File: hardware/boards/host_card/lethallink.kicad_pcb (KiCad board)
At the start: 6 copper layers, 121.2 x 98.4 mm, 217 parts, among them J1 PCIe-x4, J2 USB3_Micro_B_Amphenol, J3 Conn_02x05_Odd_Even, J4 Conn_02x04_Odd_Even, J5 Conn_02x04_Odd_Even, J6 SODIMM_260, J7 Conn_02x04_Odd_Even, Q1 Q_NMOS_GSD, Q2 Q_NMOS_GSD, Q3 Q_NMOS_GSD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

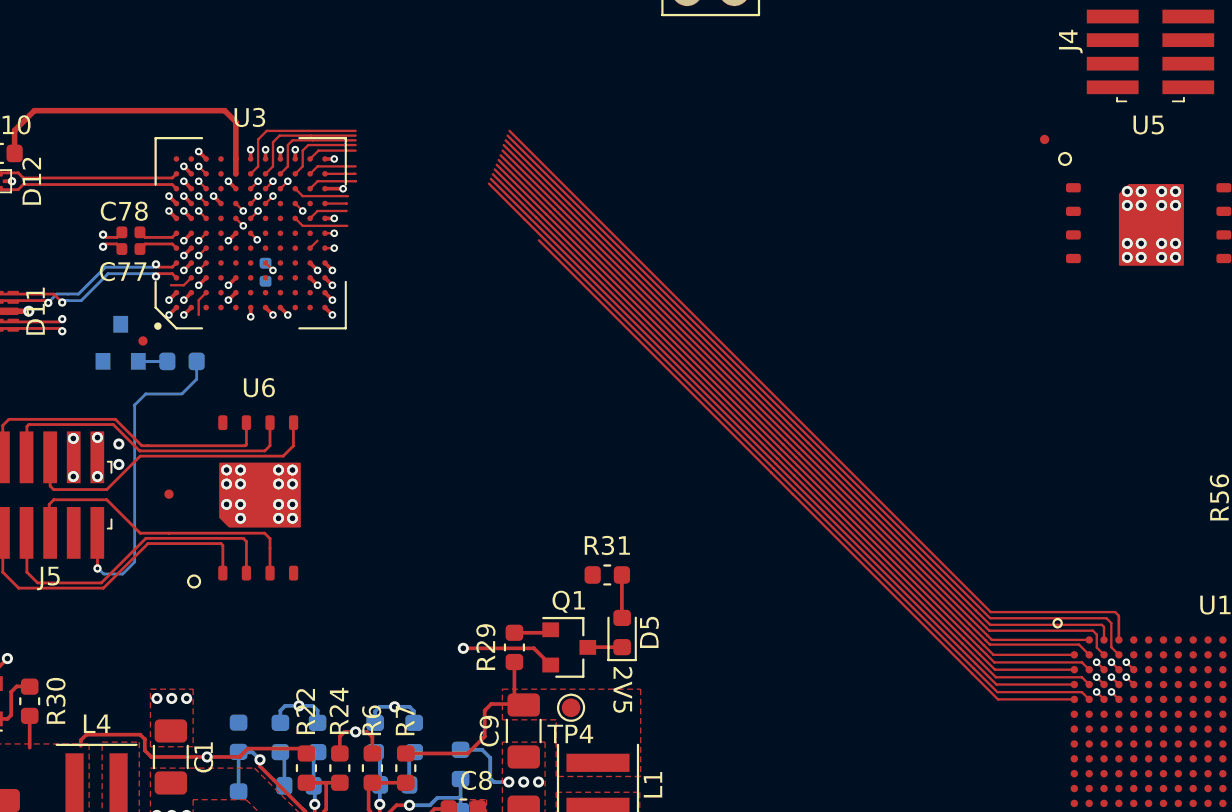
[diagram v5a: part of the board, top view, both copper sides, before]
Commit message: Wiggled all the top traces that needed a good wiggling
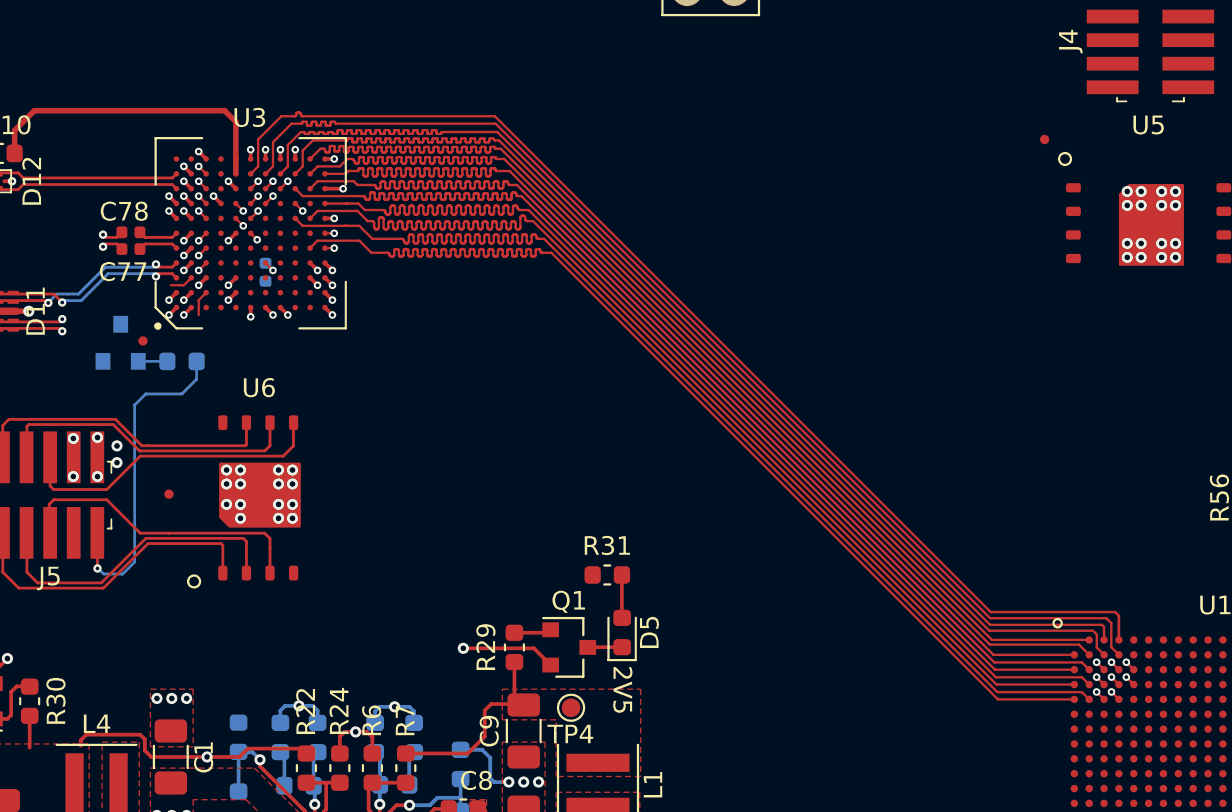
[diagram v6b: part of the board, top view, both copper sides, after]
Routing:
- net /USB3 Interface/ALE: track 39.6 -> 61.5 mm
- net /USB3 Interface/WE_D: track 44.8 -> 63.6 mm
- net /Boot Config/~PHY_INT: track 44.7 -> 62.7 mm
- net /USB3 Interface/DQ11: track 43.7 -> 61.5 mm
- net /USB3 Interface/OE: track 46.8 -> 64.4 mm
- net /USB3 Interface/DQ10: track 45.1 -> 61.6 mm
- net /USB3 Interface/DQ9: track 45.4 -> 61.5 mm
- net /USB3 Interface/DQ12: track 45.4 -> 61.5 mm
- net /USB3 Interface/DQ13: track 45.8 -> 61.5 mm
- net /USB3 Interface/DQ8: track 48.5 -> 61.5 mm
- net /USB3 Interface/DQ6: track 49.2 -> 61.6 mm
- net /USB3 Interface/DQ3: track 51.7 -> 61.5 mm
- net /USB3 Interface/DQ0: track 53.7 -> 62.8 mm

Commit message: Lots of updates from a while ago, don't recall what's changed
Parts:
- moved R38 77.5 mm to (70.0, 82.8), turned to 180 degrees
- moved R39 74.7 mm to (70.0, 84.3), turned to 180 degrees
- moved R40 71.8 mm to (70.0, 86.0), turned to 180 degrees
- moved J3 71.4 mm to (68.0, 85.2), turned to 270 degrees
- moved R41 69.0 mm to (70.0, 87.5), turned to 180 degrees
- moved J7 20.6 mm to (73.1, 57.4)
- moved J5 2.04 mm to (26.4, 75.1)
- moved FID4 2.04 mm to (32.9, 75.0)
- moved U6 2.04 mm to (37.7, 75.2)
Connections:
- J3 pad 6: Net-(J3-Pad6) -> /Boot Config/TDO
- R40 pad 2: Net-(J3-Pad6) -> /Boot Config/TDO
- U1 pad V4: /Boot Config/TDO -> /Boot Config/FPGA_TDO
- U3 pad C10: Net-(J3-Pad6) -> /Boot Config/TDO
- U3 pad E7: /Boot Config/TDO -> /Boot Config/FPGA_TDO
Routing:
- net /Boot Config/FPGA_TDO: track 0.00 -> 6.55 mm, vias 0 -> 1
- net /Boot Config/TMS: track 0.57 -> 6.55 mm
- net /USB3 Interface/DQ14: track 55.8 -> 61.6 mm
- net /Boot Config/TCK: track 0.49 -> 5.81 mm
- net /USB3 Interface/DQ7: track 57.0 -> 61.5 mm
- net /USB3 Interface/DQ15: track 57.2 -> 61.5 mm
- net /USB3 Interface/DQ5: track 57.9 -> 61.5 mm
- net /USB3 Interface/DQ2: track 59.2 -> 61.5 mm
- net /Boot Config/~PHY_RESET: track 17.7 -> 19.9 mm
- net /USB3 Interface/DQ4: track 59.6 -> 61.6 mm
- net +3V3: track 5.30 -> 6.65 mm, vias 6 -> 7
- net /USB3 Interface/DQ1: track 60.2 -> 61.5 mm
- net /Boot Config/FPGA_DI: track 16.9 -> 17.5 mm, vias 0 -> 1
- net /Boot Config/FPGA_CLK: track 16.8 -> 17.4 mm, vias 0 -> 1
- net Net-(J3-Pad6): track 0.57 -> 0.00 mm, vias 1 -> 0
